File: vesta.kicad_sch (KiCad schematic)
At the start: 42 parts, among them J1 Solar Panel, J2 Solar Panel, U1 STM32WL55CCU6, U2 BQ24074RGTR, U3 TPS63900DSKR, U4 BME688_C3664478, U5 SHT40-AD1F-R2, X1 Q13FC1350000400, Y1 32MHz

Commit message: feat: adding the clocks, the boot and the reset to the schemas
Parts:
- added C15: 100nF, symbol Device:C
- added J3: Conn_ARM_SWD_TagConnect_TC2030-NL, Connector:Tag-Connect_TC2030-IDC-NL_2x03_P1.27mm_Vertical, symbol Connector:Conn_ARM_SWD_TagConnect_TC2030-NL
- added R11: 100kΩ, symbol Device:R
- added TP3: TP_BOOT0, symbol Connector:TestPoint
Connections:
- net 3V3_SYS: now also J3.1 (VCC)
- net GND: now also C15.2, J3.5 (GND), R11.1
- net NRST: now reaches U1.18 (NRST)
- net NRST: now also C15.1, J3.3 (~{RESET})
- net PH3-BOOT0: now reaches U1.19 (PH3-BOOT0)
- net PH3-BOOT0: now also R11.2, TP3.1
- net SWDIO: now reaches U1.36 (PA13)
- net SWDIO: now also J3.2 (SWDIO)
- net SWCLK: now reaches U1.42 (PA14)
- net SWCLK: now also J3.4 (SWCLK)
- new net SWO: J3.6 (SWO)
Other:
- note added: "Boot & Reset"

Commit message: feat: adding the ST IPD and RF antenna
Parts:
- removed JP_PA_SEL: Jumper_3_Bridged12, symbol Jumper:Jumper_3_Bridged12
- added C16, C17, C18: 100pF, symbol Device:C
- added C19: 100nF, symbol Device:C
- added C20, C21: DNP, symbol Device:C
- added FL1: BALFHB-WL-05D3, JLCImport:BALFHB-WL-05D3, symbol JLCImport:BALFHB-WL-05D3
- added J4: U.FL, PCM_JLCPCB:IPEX-SMD_BWIPX-1-001E, symbol PCM_JLCPCB-Extended:RF, Connector, U.FL
- added R12: 100kΩ, symbol Device:R
- added R13: 0Ω, symbol Device:R
- added U6: PE4259-63, JLCImport:PE4259-63, symbol JLCImport:PE4259-63
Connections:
- net 3V3_SYS: now also C19.2, U6.6 (CTRL#_or_VDD)
- net GND: now also C19.1, C20.2, C21.2, FL1.B1 (GND2), FL1.B2 (GND3), FL1.C2 (GND1), J4.2 (Ext), R12.1, U6.2 (GND)
- net RFI_P_OUT: now reaches U1.20 (RFI_P)
- net RFI_P_OUT: now also FL1.A3 (RFI_P_out)
- net RFI_N_OUT: now reaches U1.21 (RFI_N)
- net RFI_N_OUT: now also FL1.A2 (RFI_N_out)
- net RFO_IN: now reaches U1.22 (RFO_LP)
- net RFO_IN: now also FL1.A1 (RFO_in)
- net RF_SW_CTRL: now reaches U1.32 (PB12)
- net RF_SW_CTRL: now also R12.2, U6.4 (CTRL)
- new net: C16.2, U6.1 (RF1)
- new net: C17.2, U6.3 (RF2)
- new net: C18.2, U6.5 (RFC)
- new net: C21.1, J4.1 (In), R13.1
- new net RFI_IN: C17.1, FL1.C3 (RFI_in)
- new net RFO_OUT: C16.1, FL1.C1 (RFO_out)
- new net RF_ANT_SW: C18.1, C20.1, R13.2
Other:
- note added: "Area | Note ----------------- | ------------------------------------------------------------------------------------------------- High-power | `RFO_HP` is not used in this design because the gains to power ratio aren't there for this use case RF switch control | `RF_SW_CTRL LOW = RX`, `RF_SW_CTRL HIGH = TX`. DC blocks | `C16/C17/C18` are RF DC-block capacitors. Use `100pF C0G/NP0`. Antenna tuning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"
- note added: "RF IPD & Antenna"
- moved on the sheet: C15, J3, R11, TP3

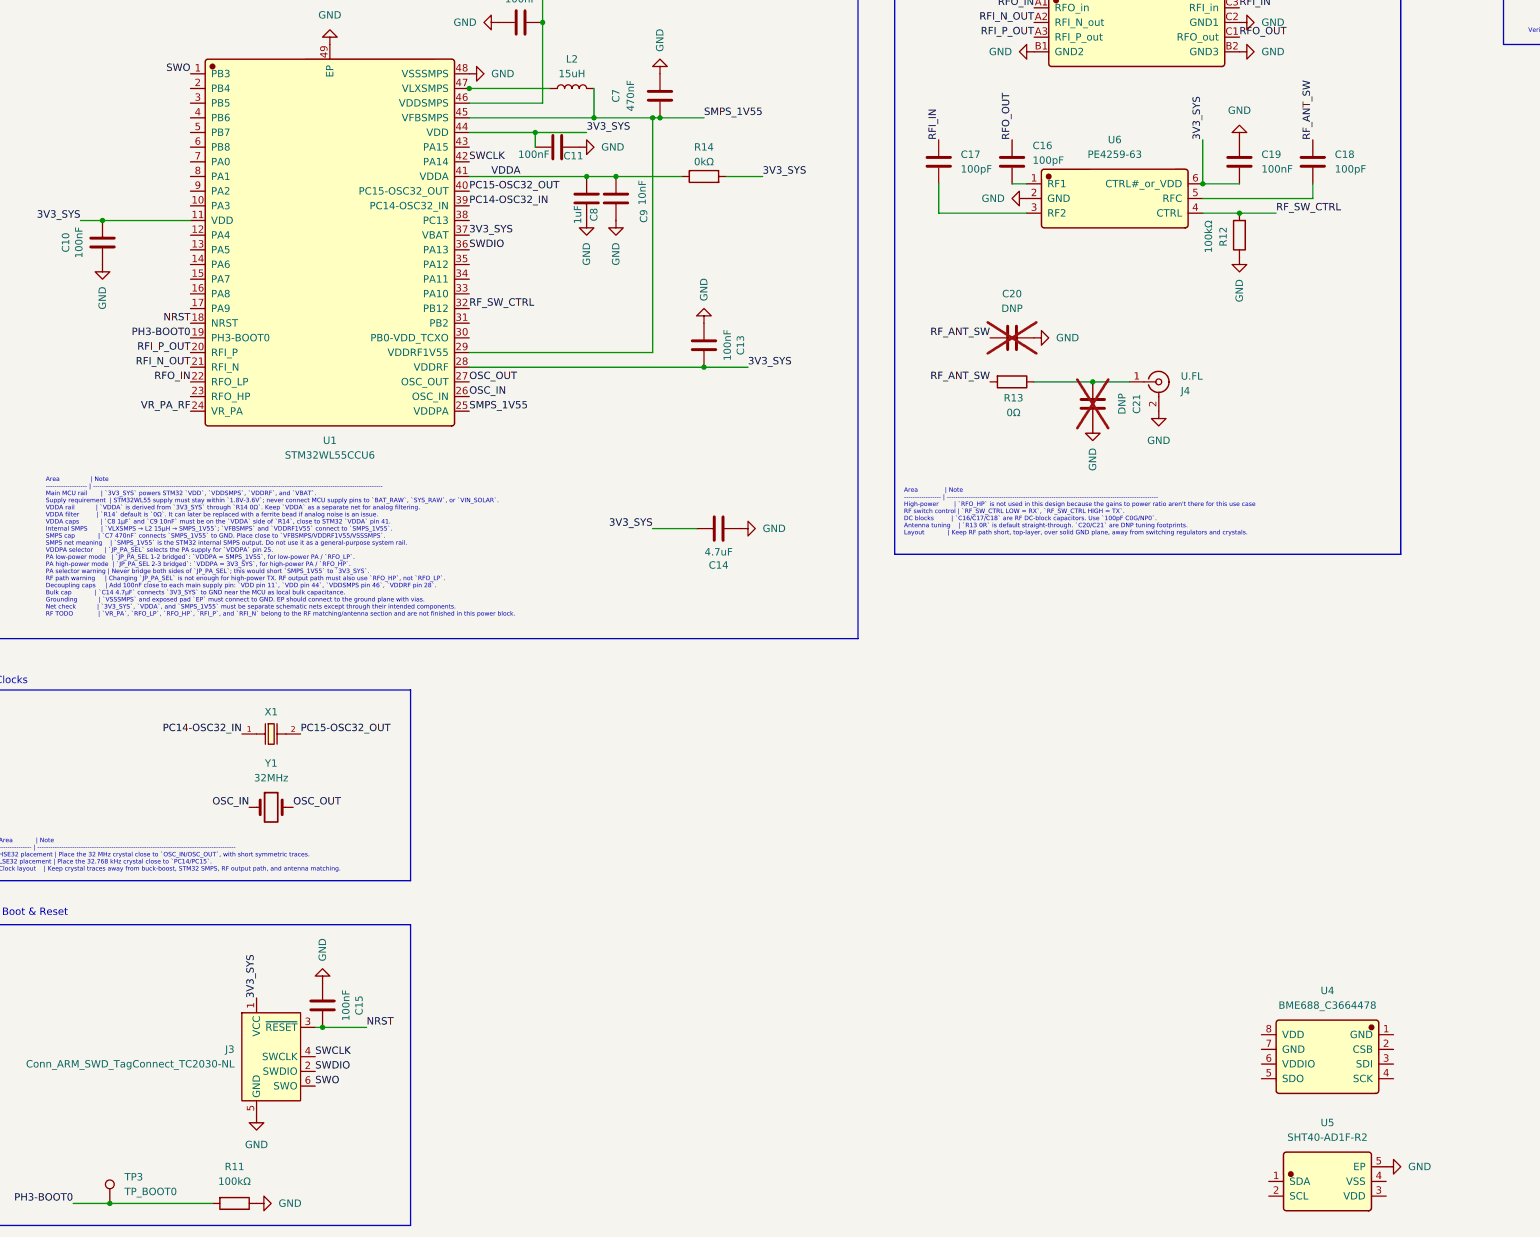
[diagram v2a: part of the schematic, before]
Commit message: feat: adding the connections to the sensor
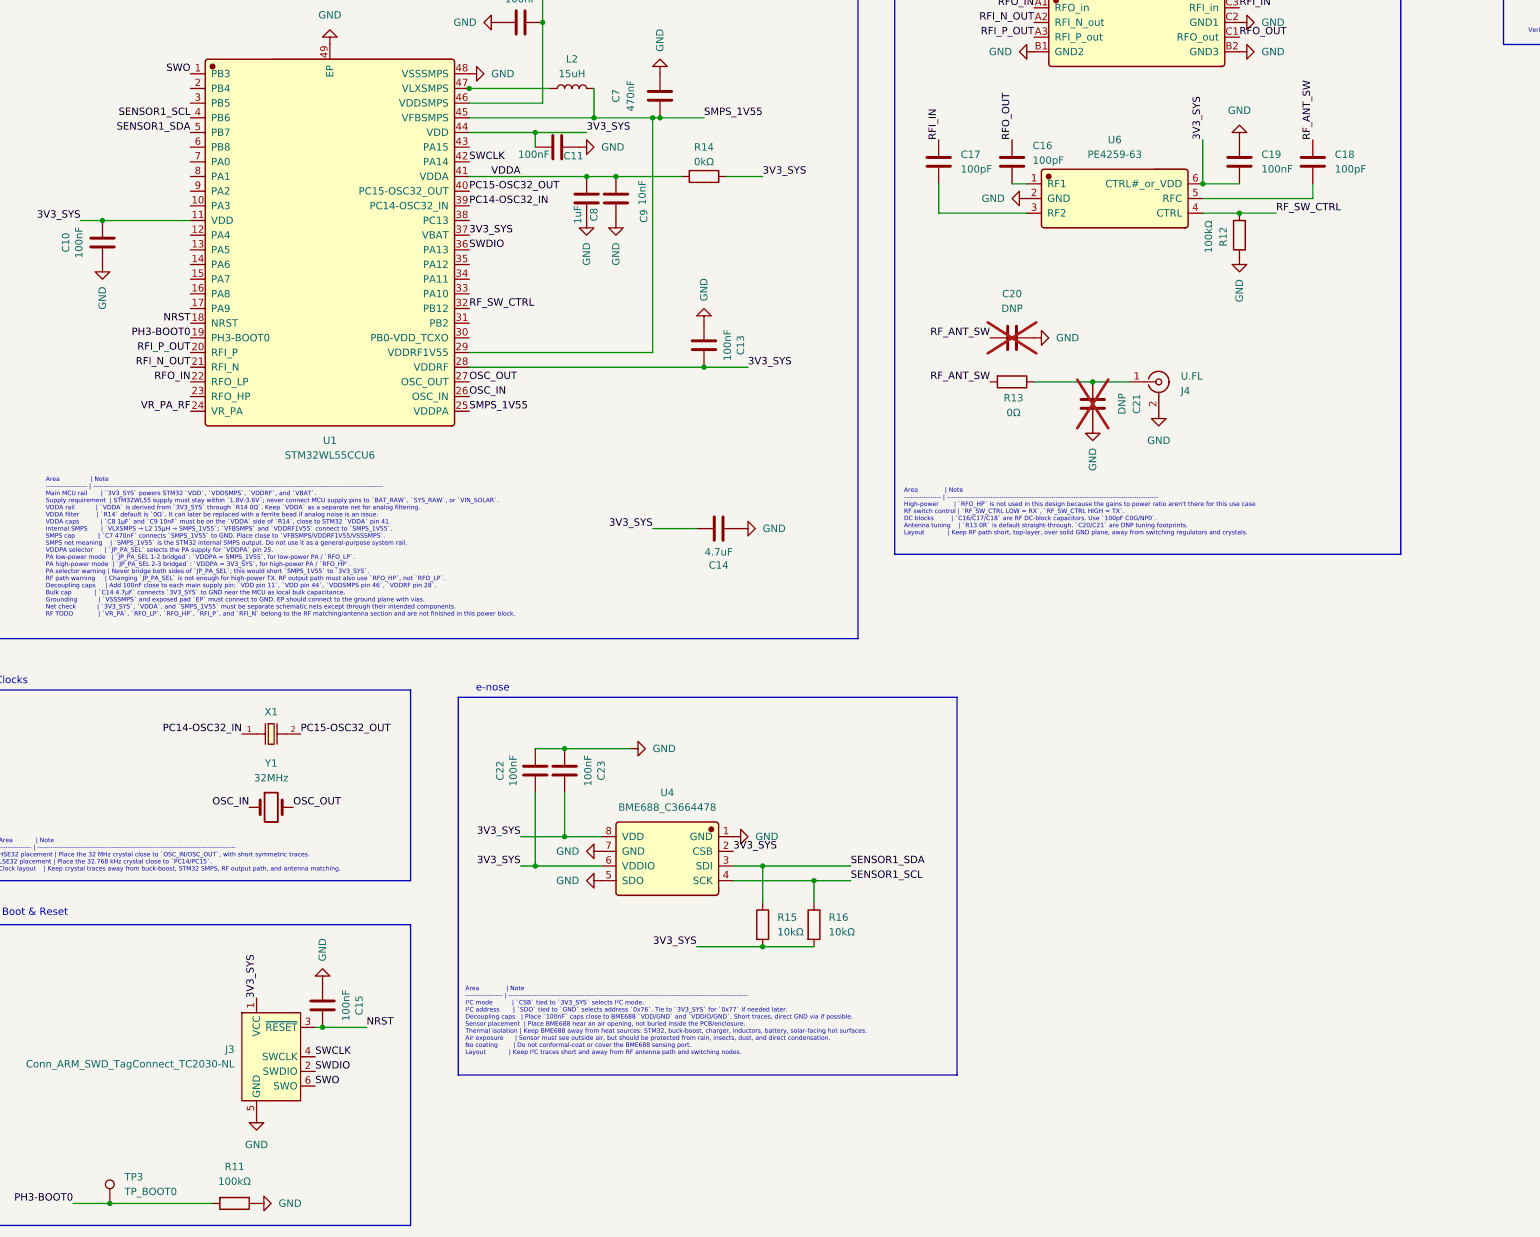
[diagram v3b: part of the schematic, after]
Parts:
- removed U5: SHT40-AD1F-R2, JLCImport:SHT40-AD1F-R2, symbol JLCImport:SHT40-AD1F-R2
- added C22, C23: 100nF, symbol Device:C
- added R15, R16: 10kΩ, symbol Device:R
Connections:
- net 3V3_SYS: now also U4.2 (CSB), U4.6 (VDDIO), U4.8 (VDD), C22.1, C23.1, R15.2, R16.2
- net GND: now also U4.1 (GND), U4.5 (SDO), U4.7 (GND), C22.2, C23.2
- net SENSOR1_SDA: now reaches U4.3 (SDI)
- net SENSOR1_SDA: now also U1.5 (PB7), R15.1
- net SENSOR1_SCL: now reaches U4.4 (SCK)
- net SENSOR1_SCL: now also U1.4 (PB6), R16.1
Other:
- note added: "Area | Note ----------------- | -------------------------------------------------------------------------------------------------------------- I²C mode | `CSB` tied to `3V3_SYS` selects I²C mode. I²C address | `SDO` tied to `GND` selects address `0x76`. Tie to `3V3_SYS` for `0x77` if needed later. Decoupling caps | Place `100nF` caps close to BME688 `VDD/GND` and `VDDIO/GND`. Short traces, direct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"
- note added: "e-nose"
- moved on the sheet: U4

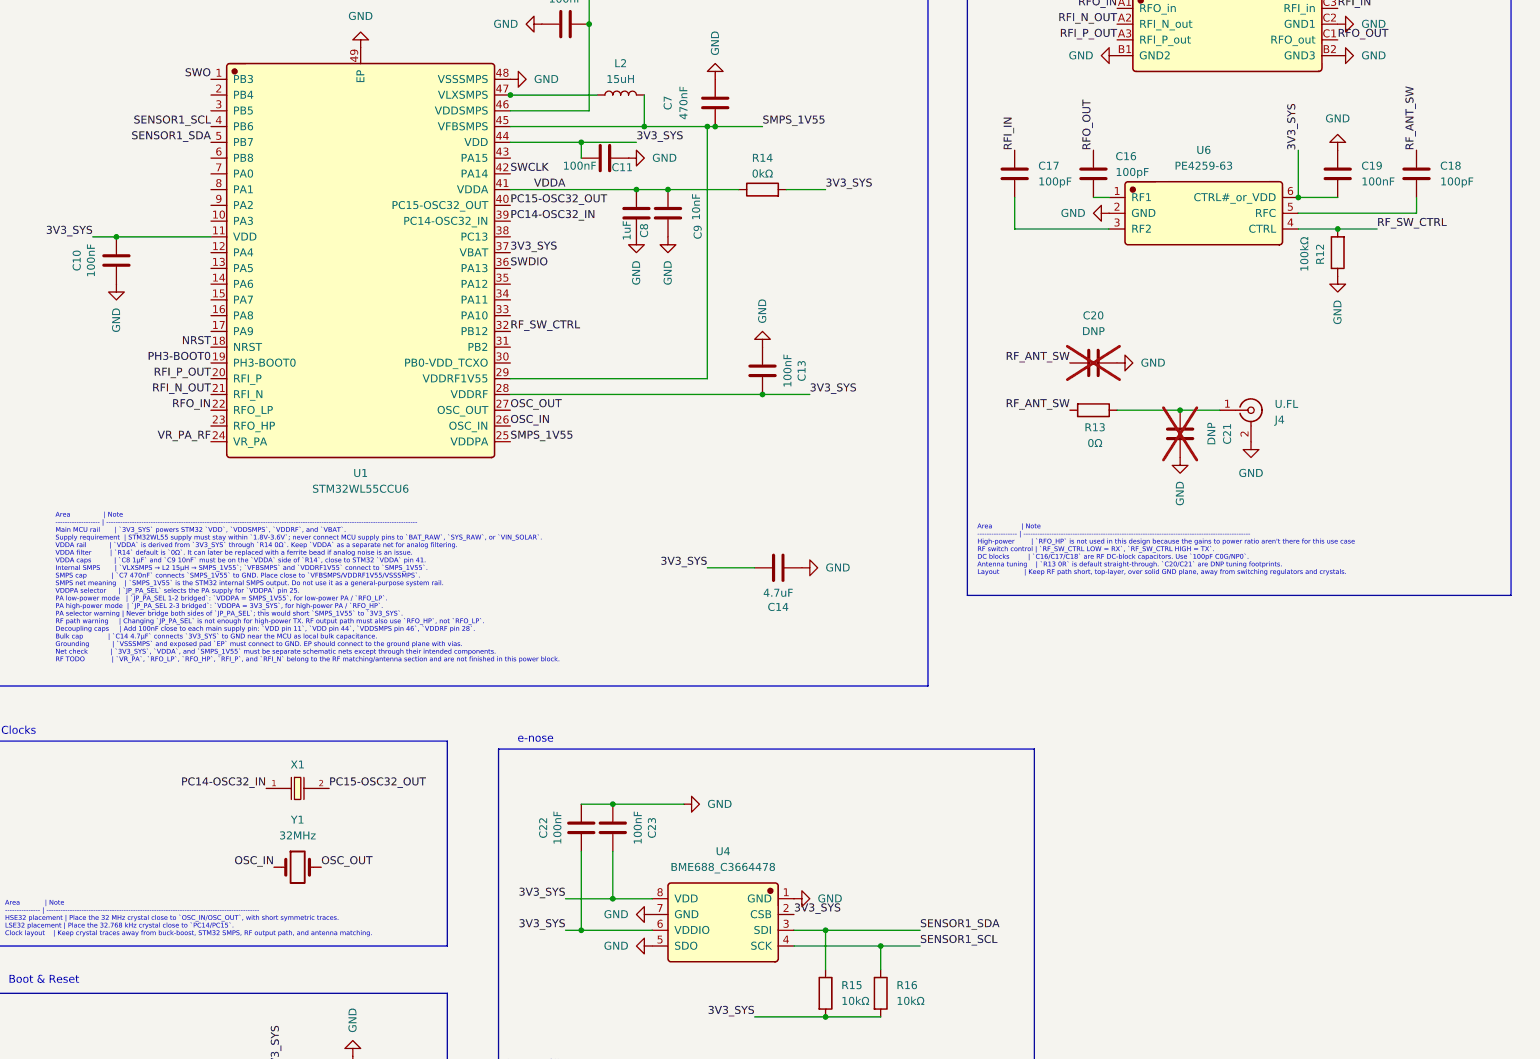
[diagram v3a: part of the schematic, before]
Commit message: feat: adding the expansion pads
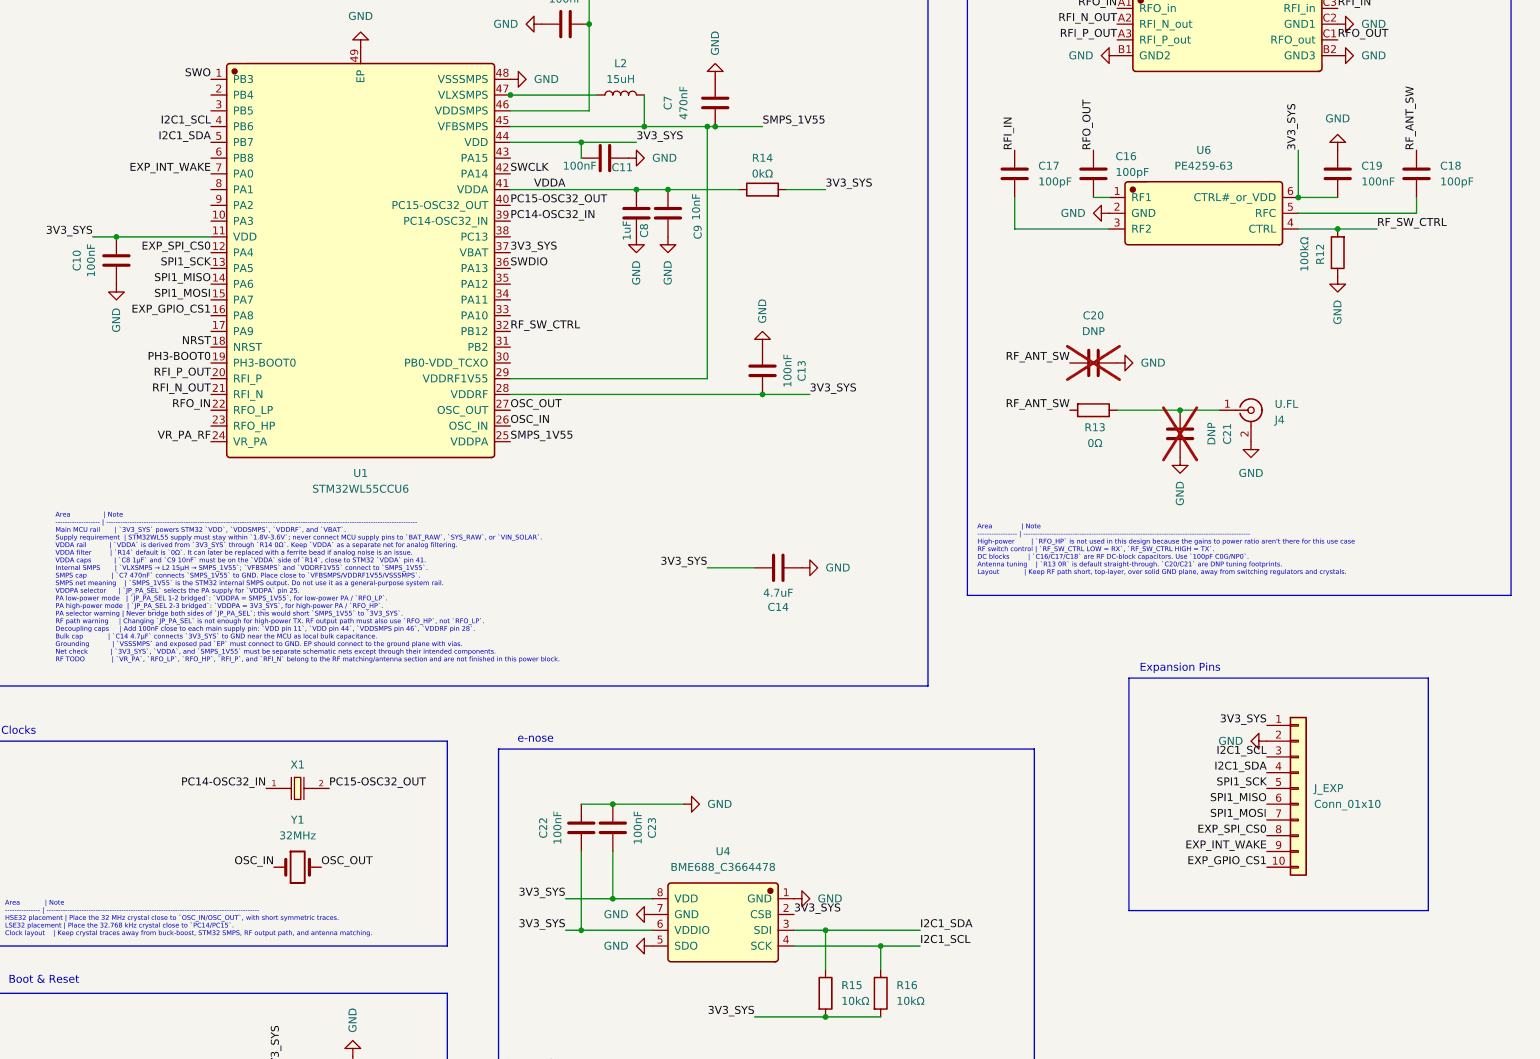
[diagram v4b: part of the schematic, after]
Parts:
- added J_EXP: Conn_01x10, Connector_PinHeader_1.00mm:PinHeader_1x10_P1.00mm_Horizontal, symbol Connector_Generic:Conn_01x10
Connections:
- net 3V3_SYS: now also J_EXP.1 (Pin_1)
- net GND: now also J_EXP.2 (Pin_2)
- net EXP_SPI_CS0: now reaches U1.12 (PA4)
- net EXP_SPI_CS0: now also J_EXP.8 (Pin_8)
- net SPI1_SCK: now reaches U1.13 (PA5)
- net SPI1_SCK: now also J_EXP.5 (Pin_5)
- net SPI1_MISO: now reaches U1.14 (PA6)
- net SPI1_MISO: now also J_EXP.6 (Pin_6)
- net SPI1_MOSI: now reaches U1.15 (PA7)
- net SPI1_MOSI: now also J_EXP.7 (Pin_7)
- net EXP_GPIO_CS1: now reaches U1.16 (PA8)
- net EXP_GPIO_CS1: now also J_EXP.10 (Pin_10)
- net EXP_INT_WAKE: now reaches U1.7 (PA0)
- net EXP_INT_WAKE: now also J_EXP.9 (Pin_9)
- net SENSOR1_SCL renamed I2C1_SCL
- net I2C1_SCL: now also J_EXP.3 (Pin_3)
- net SENSOR1_SDA renamed I2C1_SDA
- net I2C1_SDA: now also J_EXP.4 (Pin_4)
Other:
- note added: "Expansion Pins"
